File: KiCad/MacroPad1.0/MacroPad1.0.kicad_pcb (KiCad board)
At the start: 2 copper layers, 28 parts, among them SW1 SW_Push, U1 ATmega32U4-A, Y1 16MHz

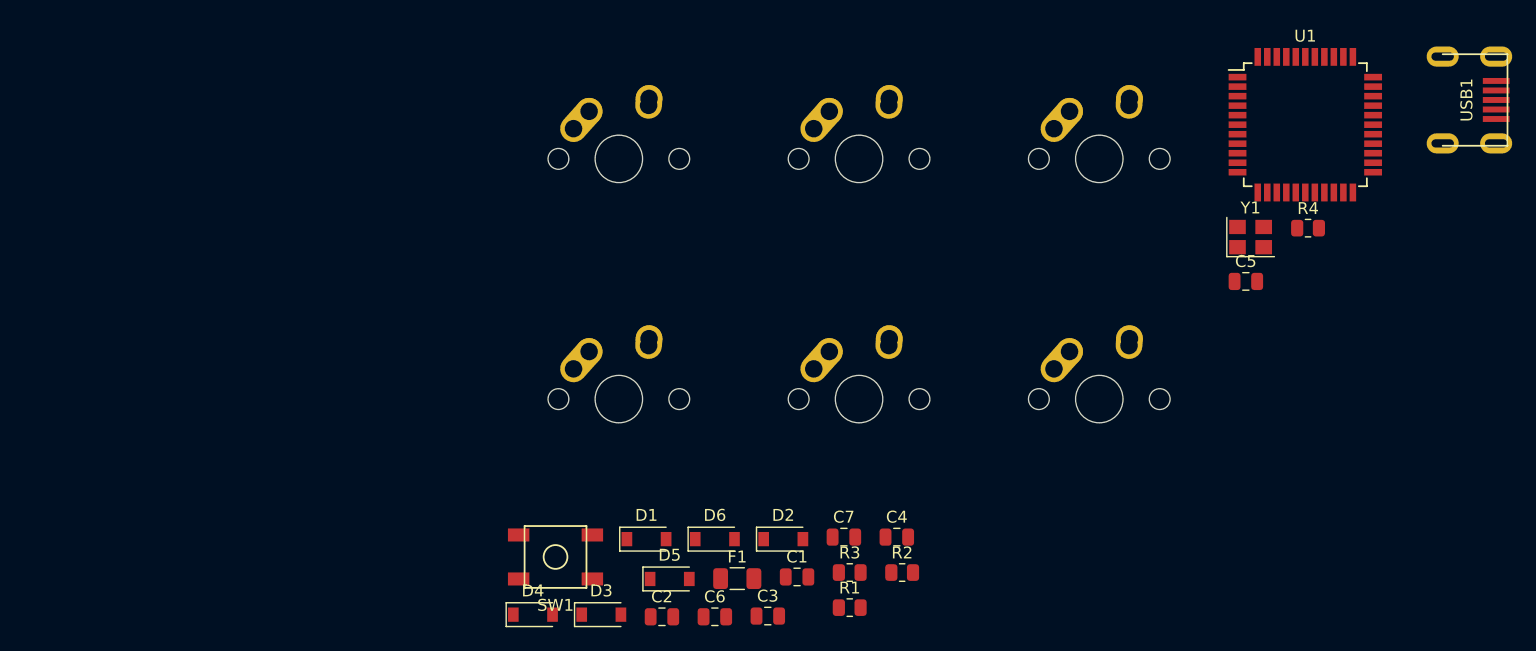
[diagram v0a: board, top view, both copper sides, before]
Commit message: PCB Layout complete
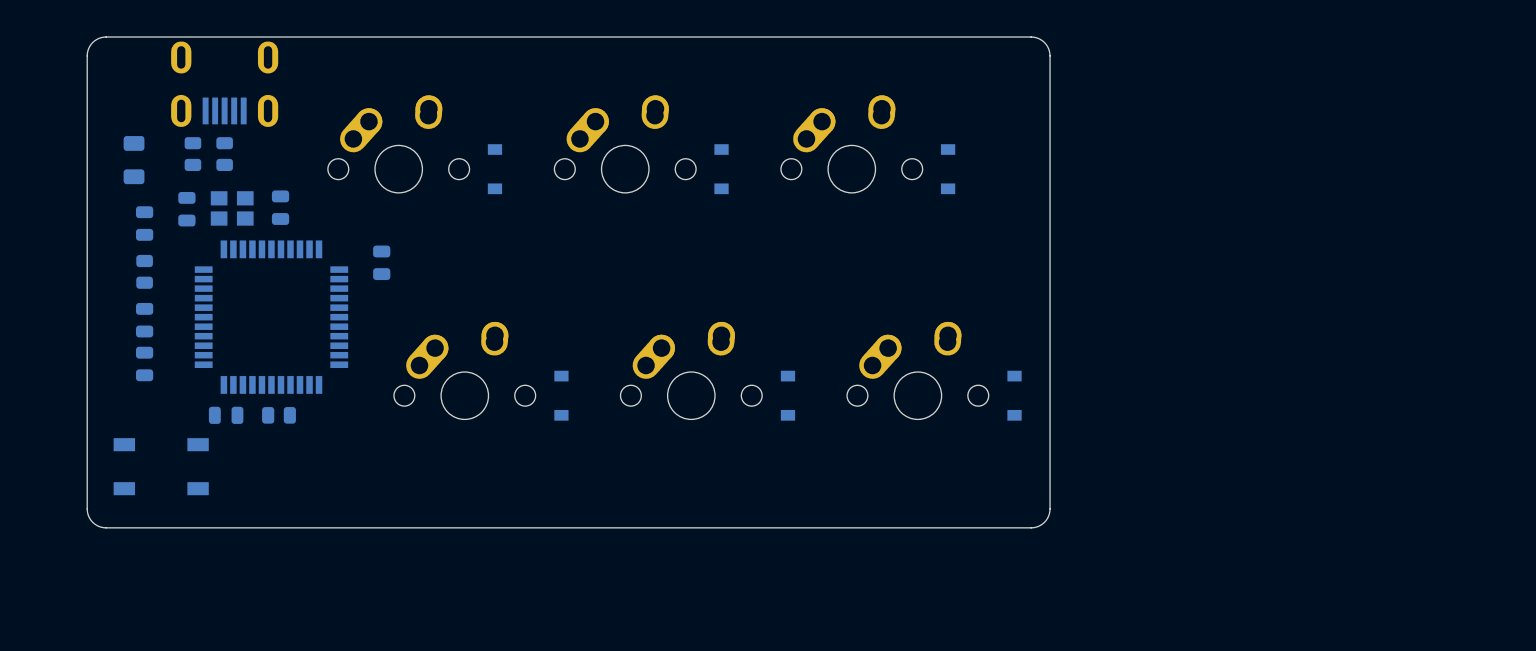
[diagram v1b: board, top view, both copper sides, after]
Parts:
- C1, C2, C3, C4, C5, C6, C7, D1, D2, D3, D4, D5, D6, F1, R1, R2, R3, R4, SW1, U1, USB1, Y1: moved to B.Cu
- moved USB1 102.5 mm to (81.4, 73.2), turned to -90 degrees
- moved U1 88.4 mm to (85.3, 95.0)
- moved R4 88.0 mm to (86.0, 103.3), turned to 180 degrees
- moved C5 86.5 mm to (81.5, 103.3)
- moved Y1 85.7 mm to (82.0, 85.9), turned to 180 degrees
- moved R1 67.1 mm to (78.7, 81.3), turned to -90 degrees
- moved R2 67.0 mm to (81.4, 81.3), turned to -90 degrees
- moved C4 64.9 mm to (74.7, 98.9), turned to 90 degrees
- moved R3 64.5 mm to (74.7, 91.2), turned to -90 degrees
- moved C3 61.9 mm to (74.7, 87.1), turned to 90 degrees
- moved F1 61.7 mm to (73.8, 81.8), turned to -90 degrees
- moved C7 61.6 mm to (74.7, 95.2), turned to -90 degrees
- moved C1 53.4 mm to (86.1, 85.8), turned to 90 degrees
- moved C2 52.6 mm to (78.2, 85.9), turned to -90 degrees
- moved D3 47.5 mm to (142.2, 82.5), turned to -90 degrees
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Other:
- board outline added: 81 x 41.3 mm

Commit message: PCB traces complete
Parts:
- moved MX2 24.9 mm to (101.6, 103.5)
- moved D2 24.9 mm to (109.7, 103.5)
- moved D5 21.8 mm to (142.2, 84.4)
- moved MX5 21.8 mm to (134.1, 84.4)
- moved D3 19.2 mm to (123.2, 84.4)
- moved MX3 19.2 mm to (115.1, 84.4)
- moved MX4 19.1 mm to (120.7, 103.5)
- moved D4 19.1 mm to (128.8, 103.5)
- moved R4 7.35 mm to (88.4, 110.2)
- moved C5 7.35 mm to (83.9, 110.2)
- moved C2 7.13 mm to (84.8, 88.6)
- moved U1 4.79 mm to (85.3, 99.8)
- moved C1 3.88 mm to (88.8, 88.6)
- moved Y1 2.99 mm to (80.9, 88.6)
- moved C3 2.63 mm to (72.8, 88.9)
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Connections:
- U1 pad 26: unconnected-(U1-Pad26) -> Col2
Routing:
- net +5V: track 0.00 -> 123.3 mm, vias 0 -> 14
- net GND: track 0.00 -> 106.5 mm, vias 0 -> 11
- net Row0: track 0.00 -> 90.5 mm, vias 0 -> 4
- net Row1: track 0.00 -> 80.2 mm, vias 0 -> 4
- net Col2: track 0.00 -> 68.4 mm, vias 0 -> 2
- net Col1: track 0.00 -> 49.4 mm, vias 0 -> 2
- net Net-(R3-Pad1): track 0.00 -> 35.1 mm, vias 0 -> 3
- net Col0: track 0.00 -> 28.2 mm, vias 0 -> 1
- net Net-(R2-Pad2): track 0.00 -> 24.8 mm, vias 0 -> 2
- net Net-(R1-Pad2): track 0.00 -> 24.7 mm, vias 0 -> 6
- net Net-(C3-Pad1): track 0.00 -> 18.6 mm
- net VCC: track 0.00 -> 9.35 mm
- net Net-(C7-Pad1): track 0.00 -> 8.74 mm, vias 0 -> 2
- net Net-(D6-Pad2): track 0.00 -> 8.48 mm
- net Net-(D5-Pad2): track 0.00 -> 8.48 mm
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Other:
- board size 81 x 41.3 mm -> 90.5 x 46 mm

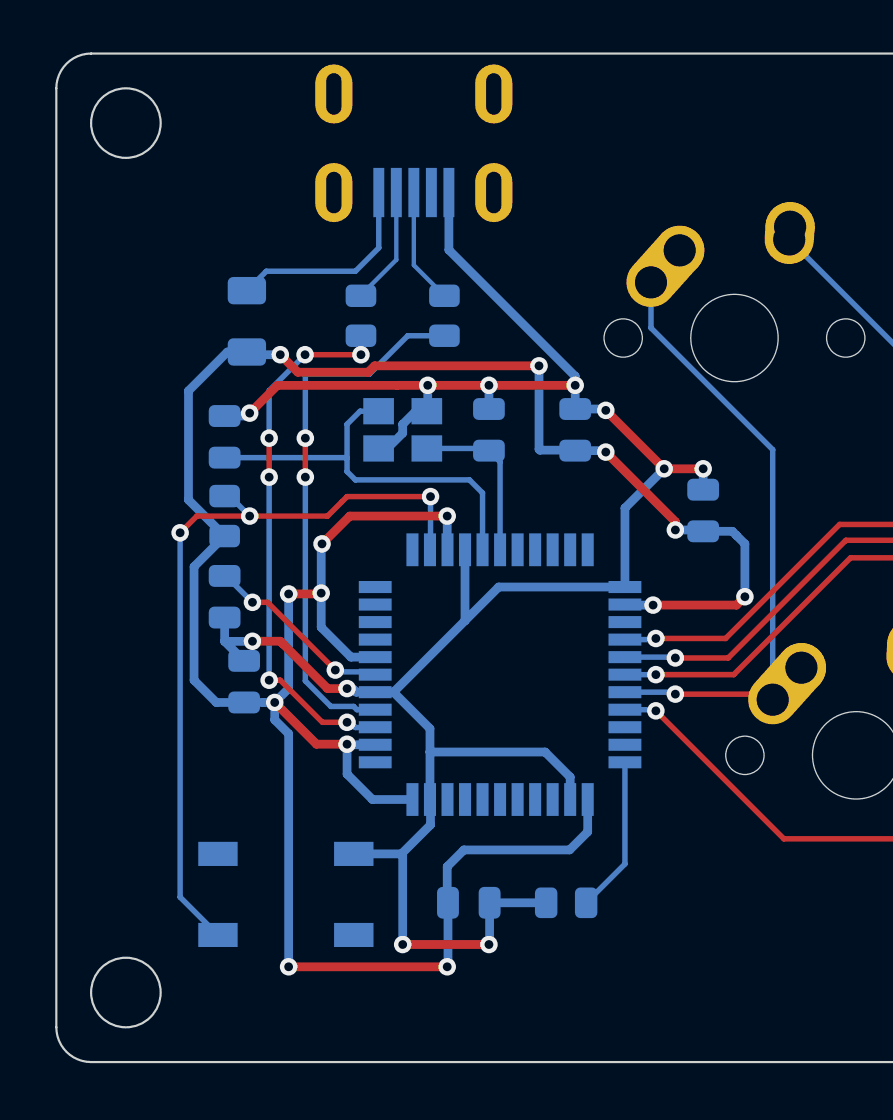
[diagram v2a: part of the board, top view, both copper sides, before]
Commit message: Added ground mask & screenshot
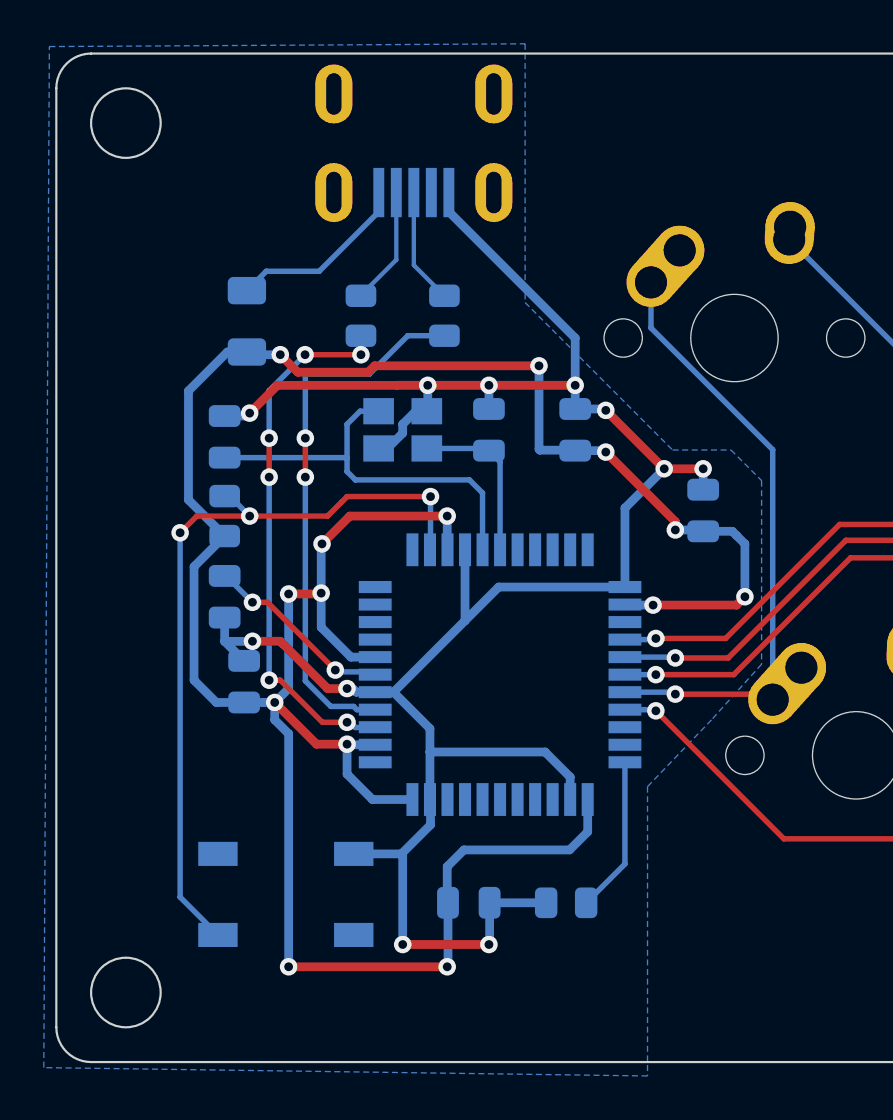
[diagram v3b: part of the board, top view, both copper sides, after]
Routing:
- net VCC: track 9.35 -> 8.39 mm
- added copper zone on B.Cu, net GND
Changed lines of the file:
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@@
   (segment (start 78.665 107.97325) (end 80.844 107.97325) (width 0.4) (layer "B.Cu") (net 2))
   (segment (start 74.036 98.27125) (end 74.041 98.26625) (width 0.4) (layer "B.Cu") (net 2))
-  (segment (start 88.773 86.16975) (end 83.007 80.40375) (width 0.4) (layer "B.Cu") (net 2))
   (segment (start 84.866 110.20425) (end 87.4485 110.20425) (width 0.4) (layer "B.Cu") (net 2))
   (segment (start 80.899 88.76425) (end 80.199 89.46425) (width 0.4) (layer "B.Cu") (net 2))
@@
   (segment (start 72.771 97.18425) (end 72.771 98.27125) (width 0.4) (layer "B.Cu") (net 2))
   (segment (start 94.549 91.28125) (end 94.615 91.34725) (width 0.4) (layer "B.Cu") (net 2))
+  (segment (start 83.007 77.7825) (end 83.007 78.6575) (width 0.4) (layer "B.Cu") (net 2))
   (segment (start 80.844 107.97325) (end 82.169 106.64825) (width 0.4) (layer "B.Cu") (net 2))
   (segment (start 80.899 108.02825) (end 80.844 107.97325) (width 0.4) (layer "B.Cu") (net 2))
@@
   (segment (start 84.866 112.07925) (end 84.836 112.10925) (width 0.4) (layer "B.Cu") (net 2))
   (segment (start 82.042 87.72125) (end 81.999 87.76425) (width 0.4) (layer "B.Cu") (net 2))
+  (segment (start 88.773 84.4235) (end 88.773 86.58225) (width 0.4) (layer "B.Cu") (net 2))
   (segment (start 94.615 90.39225) (end 94.615 91.34725) (width 0.4) (layer "B.Cu") (net 2))
   (segment (start 82.042 86.58225) (end 82.042 87.72125) (width 0.4) (layer "B.Cu") (net 2))
@@
   (segment (start 88.773 87.66425) (end 90.109 87.66425) (width 0.4) (layer "B.Cu") (net 2))
   (segment (start 91.044 95.79025) (end 85.28 95.79025) (width 0.4) (layer "B.Cu") (net 2))
-  (segment (start 88.773 86.58225) (end 88.773 86.16975) (width 0.4) (layer "B.Cu") (net 2))
   (segment (start 84.836 87.66425) (end 84.836 86.58225) (width 0.4) (layer "B.Cu") (net 2))
   (segment (start 88.544 105.49025) (end 88.544 104.46525) (width 0.4) (layer "B.Cu") (net 2))
+  (segment (start 83.007 78.6575) (end 88.773 84.4235) (width 0.4) (layer "B.Cu") (net 2))
   (segment (start 88.773 87.66425) (end 88.773 86.58225) (width 0.4) (layer "B.Cu") (net 2))
   (segment (start 82.144 103.32125) (end 82.144 102.25425) (width 0.4) (layer "B.Cu") (net 2))
-  (segment (start 83.007 80.40375) (end 83.007 77.7825) (width 0.4) (layer "B.Cu") (net 2))
   (segment (start 84.866 110.20425) (end 84.866 112.07925) (width 0.4) (layer "B.Cu") (net 2))
   (segment (start 85.28 95.79025) (end 83.744 97.32625) (width 0.4) (layer "B.Cu") (net 2))
@@
   (segment (start 142.2 98.97325) (end 147.828 104.60125) (width 0.25) (layer "B.Cu") (net 13))
   (segment (start 147.828 104.60125) (end 147.828 105.12325) (width 0.25) (layer "B.Cu") (net 13))
-  (segment (start 74.673 81.37525) (end 78.74 81.37525) (width 0.25) (layer "B.Cu") (net 14))
-  (segment (start 78.74 81.37525) (end 79.807 80.30825) (width 0.25) (layer "B.Cu") (net 14))
-  (segment (start 79.807 80.30825) (end 79.807 77.7825) (width 0.25) (layer "B.Cu") (net 14))
+  (segment (start 74.673 81.37525) (end 77.08925 81.37525) (width 0.25) (layer "B.Cu") (net 14))
+  (segment (start 77.08925 81.37525) (end 79.807 78.6575) (width 0.25) (layer "B.Cu") (net 14))
+  (segment (start 79.807 78.6575) (end 79.807 77.7825) (width 0.25) (layer "B.Cu") (net 14))
   (segment (start 73.787 82.26125) (end 74.673 81.37525) (width 0.25) (layer "B.Cu") (net 14))
   (segment (start 93.345 100.67925) (end 97.536 100.67925) (width 0.25) (layer "F.Cu") (net 15))
@@
   (segment (start 89.2735 110.20425) (end 91.044 108.43375) (width 0.25) (layer "B.Cu") (net 23))
   (segment (start 91.044 108.43375) (end 91.044 103.79025) (width 0.25) (layer "B.Cu") (net 23))
+  (zone (net 2) (net_name "GND") (layer "B.Cu") (hatch edge 0.508)
+    (connect_pads (clearance 0.508))
+    (min_thickness 0.254) (filled_areas_thickness no)
+    (fill yes (thermal_gap 0.508) (thermal_bridge_width 0.508))
+    (polygon
+      (pts
+        (xy 86.487 70.993)
+        (xy 86.487 82.804)
+        (xy 93.218 89.535)
+        (xy 95.885 89.535)
+        (xy 97.282 90.932)
+        (xy 97.282 99.314)
+        (xy 94.996 101.854)
+        (xy 92.075 104.902)
+        (xy 92.075 118.11)
+        (xy 64.516 117.729)
+        (xy 64.77 71.12)
+        (xy 64.77 71.12)
+      )
+    )
+  )
 )

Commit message: Adjusted Traces
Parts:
- moved C3 4.07 mm to (76.8, 88.6)
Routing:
- net Net-(C3-Pad1): track 18.6 -> 14.6 mm
- net GND: track 106.5 -> 102.9 mm
- net Net-(R2-Pad2): track 24.8 -> 25.6 mm, vias 2 -> 0
- net +5V: track 123.3 -> 122.8 mm
- net Net-(R1-Pad2): vias 6 -> 4
